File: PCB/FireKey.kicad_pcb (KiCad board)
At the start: 2 copper layers, 3.6 x 3.2 mm, 76 parts, among them SW1 SW_MEC_5E, U1 Arduino_Pro_Micro_USB-C

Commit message: worked on pcb design
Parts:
- moved H7 208.2 mm to (66.0, 58.4)
- moved KEY3 176.0 mm to (196.0, -91.6)
- moved C10 172.5 mm to (233.9, -92.0)
- moved KEY13 155.8 mm to (155.6, -71.4)
- moved KEY9 149.7 mm to (117.2, -51.2)
- moved C4 126.9 mm to (173.1, -29.4)
- moved C1 123.2 mm to (152.2, -11.2)
- moved C15 123.2 mm to (179.6, -35.5)
- moved C3 123.2 mm to (213.9, -71.8)
- moved C7 123.2 mm to (233.9, -89.5)
- moved C8 123.2 mm to (152.2, -8.69)
- moved C9 123.2 mm to (157.9, -14.5)
- moved D10 123.2 mm to (206.5, -62.0)
- moved D2 123.2 mm to (168.0, -29.0)
- moved D5 123.2 mm to (192.2, -54.5)
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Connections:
- KEY1 pad 1: Net-(D1-Pad2) -> Net-(D3-Pad2)
- KEY1 pad 2: Net-(D1-Pad2) -> Net-(D3-Pad2)
- KEY13 pad 1: Net-(D13-Pad2) -> Net-(D15-Pad2)
- KEY13 pad 2: Net-(D13-Pad2) -> Net-(D15-Pad2)
- KEY15 pad 1: Net-(D15-Pad2) -> Net-(D13-Pad2)
- KEY15 pad 2: Net-(D15-Pad2) -> Net-(D13-Pad2)
- KEY3 pad 1: Net-(D3-Pad2) -> Net-(D1-Pad2)
- KEY3 pad 2: Net-(D3-Pad2) -> Net-(D1-Pad2)
- KEY7 pad 1: Net-(D7-Pad2) -> Net-(D9-Pad2)
- KEY7 pad 2: Net-(D7-Pad2) -> Net-(D9-Pad2)
- KEY9 pad 1: Net-(D9-Pad2) -> Net-(D7-Pad2)
- KEY9 pad 2: Net-(D9-Pad2) -> Net-(D7-Pad2)
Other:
- board size 3.6 x 3.2 mm -> 100 x 96.5 mm

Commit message: worked on pcb design
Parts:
- moved H8 228.8 mm to (119.4, 143.5)
- moved H6 198.3 mm to (57.1, 99.1)
- moved H11 179.3 mm to (149.5, 143.5)
- moved H9 175.1 mm to (57.1, 143.5)
- moved H12 109.2 mm to (119.4, 54.6)
- moved H5 73.0 mm to (196.8, 22.9)
- moved H10 66.5 mm to (149.5, 54.6)
- moved H7 9.67 mm to (57.1, 54.6)
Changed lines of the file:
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@@
   )
   (footprint "MountingHole:MountingHole_3.2mm_M3" (layer "F.Cu")
-    (at 185.305 -52.225)
+    (at 57.15 99.06)
     (descr "Mounting Hole 3.2mm, no annular, M3")
     (tags "mounting hole 3.2mm no annular m3")
@@
     (property "exclude_from_bom" "")
     (attr exclude_from_pos_files exclude_from_bom)
-    (fp_text reference "H6" (at 0 -4.2) (layer "F.SilkS")
+    (fp_text reference "H6" (at 0 -4.2) (layer "F.SilkS") hide
       (effects (font (size 1 1) (thickness 0.15)))
     )
@@
   )
   (footprint "MountingHole:MountingHole_3.2mm_M3" (layer "F.Cu")
-    (at 138.055 -11.825)
+    (at 57.15 143.51)
     (descr "Mounting Hole 3.2mm, no annular, M3")
     (tags "mounting hole 3.2mm no annular m3")
@@
     (property "exclude_from_bom" "")
     (attr exclude_from_pos_files exclude_from_bom)
-    (fp_text reference "H9" (at 0 -4.2) (layer "F.SilkS")
+    (fp_text reference "H9" (at 0 -4.2) (layer "F.SilkS") hide
       (effects (font (size 1 1) (thickness 0.15)))
     )
@@
   )
   (footprint "MountingHole:MountingHole_3.2mm_M3" (layer "F.Cu")
-    (at 66.04 58.42)
+    (at 57.15 54.61)
     (descr "Mounting Hole 3.2mm, no annular, M3")
     (tags "mounting hole 3.2mm no annular m3")
@@
   )
   (footprint "MountingHole:MountingHole_3.2mm_M3" (layer "F.Cu")
-    (at 207.575 -67.625)
+    (at 119.38 143.51)
     (descr "Mounting Hole 3.2mm, no annular, M3")
     (tags "mounting hole 3.2mm no annular m3")
@@
     (property "exclude_from_bom" "")
     (attr exclude_from_pos_files exclude_from_bom)
-    (fp_text reference "H8" (at 0 -4.2) (layer "F.SilkS")
+    (fp_text reference "H8" (at 0 -4.2) (layer "F.SilkS") hide
       (effects (font (size 1 1) (thickness 0.15)))
     )
@@
   )
   (footprint "MountingHole:MountingHole_3.2mm_M3" (layer "F.Cu")
-    (at 177.205 -47.425)
+    (at 196.85 22.86)
     (descr "Mounting Hole 3.2mm, no annular, M3")
     (tags "mounting hole 3.2mm no annular m3")
@@
     (property "exclude_from_bom" "")
     (attr exclude_from_pos_files exclude_from_bom)
-    (fp_text reference "H5" (at 0 -4.2) (layer "F.SilkS")
+    (fp_text reference "H5" (at 0 -4.2) (layer "F.SilkS") hide
       (effects (font (size 1 1) (thickness 0.15)))
     )
@@
   )
   (footprint "MountingHole:MountingHole_3.2mm_M3" (layer "F.Cu")
-    (at 146.005 -11.825)
+    (at 149.51 54.61)
     (descr "Mounting Hole 3.2mm, no annular, M3")
     (tags "mounting hole 3.2mm no annular m3")
@@
     (property "exclude_from_bom" "")
     (attr exclude_from_pos_files exclude_from_bom)
-    (fp_text reference "H10" (at 0 -4.2) (layer "F.SilkS")
+    (fp_text reference "H10" (at 0 -4.2) (layer "F.SilkS") hide
       (effects (font (size 1 1) (thickness 0.15)))
     )
@@
   )
   (footprint "MountingHole:MountingHole_3.2mm_M3" (layer "F.Cu")
-    (at 169.105 -42.625)
+    (at 119.38 54.61)
     (descr "Mounting Hole 3.2mm, no annular, M3")
     (tags "mounting hole 3.2mm no annular m3")
@@
     (property "exclude_from_bom" "")
     (attr exclude_from_pos_files exclude_from_bom)
-    (fp_text reference "H12" (at 0 -4.2) (layer "F.SilkS")
+    (fp_text reference "H12" (at 0 -4.2) (layer "F.SilkS") hide
       (effects (font (size 1 1) (thickness 0.15)))
     )
@@
   )
   (footprint "MountingHole:MountingHole_3.2mm_M3" (layer "F.Cu")
-    (at 169.105 -34.675)
+    (at 149.51 143.51)
     (descr "Mounting Hole 3.2mm, no annular, M3")
     (tags "mounting hole 3.2mm no annular m3")
@@
     (property "exclude_from_bom" "")
     (attr exclude_from_pos_files exclude_from_bom)
-    (fp_text reference "H11" (at 0 -4.2) (layer "F.SilkS")
+    (fp_text reference "H11" (at 0 -4.2) (layer "F.SilkS") hide
       (effects (font (size 1 1) (thickness 0.15)))
     )
@@
     )
   )
-  (gr_arc locked (start 55.88 147.32) (mid 53.75868 146.44132) (end 52.88 144.32) (layer "Edge.Cuts") (width 0.2))
-  (gr_line locked (start 55.88 50.8) (end 149.86 50.8) (layer "Edge.Cuts") (width 0.2))
-  (gr_line locked (start 152.86 144.32) (end 152.86 53.8) (layer "Edge.Cuts") (width 0.2))
-  (gr_arc locked (start 149.86 50.8) (mid 151.98132 51.67868) (end 152.86 53.8) (layer "Edge.Cuts") (width 0.2))
-  (gr_arc locked (start 152.86 144.32) (mid 151.98132 146.44132) (end 149.86 147.32) (layer "Edge.Cuts") (width 0.2))
-  (gr_line locked (start 149.86 147.32) (end 55.88 147.32) (layer "Edge.Cuts") (width 0.2))
-  (gr_arc locked (start 52.88 53.8) (mid 53.75868 51.67868) (end 55.88 50.8) (layer "Edge.Cuts") (width 0.2))
-  (gr_line locked (start 52.88 53.8) (end 52.88 144.32) (layer "Edge.Cuts") (width 0.2))
+  (gr_arc locked (start 56.34 147.32) (mid 54.21868 146.44132) (end 53.34 144.32) (layer "Edge.Cuts") (width 0.2))
+  (gr_line locked (start 56.34 50.8) (end 150.32 50.8) (layer "Edge.Cuts") (width 0.2))
+  (gr_line locked (start 153.32 144.32) (end 153.32 53.8) (layer "Edge.Cuts") (width 0.2))
+  (gr_arc locked (start 150.32 50.8) (mid 152.44132 51.67868) (end 153.32 53.8) (layer "Edge.Cuts") (width 0.2))
+  (gr_arc locked (start 153.32 144.32) (mid 152.44132 146.44132) (end 150.32 147.32) (layer "Edge.Cuts") (width 0.2))
+  (gr_line locked (start 150.32 147.32) (end 56.34 147.32) (layer "Edge.Cuts") (width 0.2))
+  (gr_arc locked (start 53.34 53.8) (mid 54.21868 51.67868) (end 56.34 50.8) (layer "Edge.Cuts") (width 0.2))
+  (gr_line locked (start 53.34 53.8) (end 53.34 144.32) (layer "Edge.Cuts") (width 0.2))
 )

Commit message: moved main components on pcb
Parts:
- H10, H11, H12, H5, H6, H7, H8, H9: value M3_MountingHole -> M3_Hole
- moved KEY14 229.4 mm to (90.2, 132.1)
- moved KEY4 220.9 mm to (71.1, 74.9)
- moved KEY12 215.2 mm to (109.2, 113.0)
- moved KEY10 212.1 mm to (71.1, 113.0)
- moved KEY11 209.6 mm to (90.2, 113.0)
- moved KEY13 208.7 mm to (109.2, 132.1)
- moved OLED1 203.0 mm to (134.6, 121.9)
- moved KEY8 196.8 mm to (90.2, 94.0)
- moved KEY3 193.3 mm to (71.1, 55.9)
- moved KEY15 169.4 mm to (71.1, 132.1)
- moved KEY9 152.3 mm to (71.1, 94.0)
- moved KEY6 148.6 mm to (109.2, 74.9)
- moved KEY5 134.7 mm to (90.2, 74.9)
- moved KEY7 128.1 mm to (109.2, 94.0)
- moved KEY2 126.5 mm to (90.2, 55.9)
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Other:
- board text added: "JLCJLCJLCJLC"

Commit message: worked on placing parts on pcb
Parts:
- C1, C10, C11, C12, C13, C14, C15, C2, C3, C4, C5, C6, C7, C8, C9, D1, D10, D11, D12, D13, D14, D15, D2, D3, D4, D5, D6, D7, D8, D9, LED1, LED10, LED11, LED12, LED13, LED14, LED15, LED2, LED3, LED4, LED5, LED6, LED7, LED8, LED9, R1: moved to B.Cu
- moved C10 268.2 mm to (75.8, 124.6)
- moved LED10 242.0 mm to (68.6, 123.8)
- moved C7 235.6 mm to (99.4, 104.0), turned to 180 degrees
- moved C11 235.5 mm to (94.9, 124.6)
- moved LED15 224.9 mm to (68.6, 142.9), turned to 180 degrees
- moved C15 213.7 mm to (62.1, 143.0), turned to -90 degrees
- moved C5 213.1 mm to (94.9, 86.5)
- moved C2 209.0 mm to (80.4, 65.9), turned to 180 degrees
- moved D13 206.6 mm to (186.7, 106.0), turned to 180 degrees
- moved C3 205.5 mm to (61.3, 65.9), turned to 180 degrees
- moved LED13 202.0 mm to (106.7, 142.9), turned to 180 degrees
- moved D8 196.0 mm to (192.4, 106.0), turned to 180 degrees
- moved C13 190.8 mm to (99.4, 142.1), turned to 180 degrees
- moved C14 189.3 mm to (80.4, 142.1), turned to 180 degrees
- moved LED12 188.5 mm to (106.7, 123.8)
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
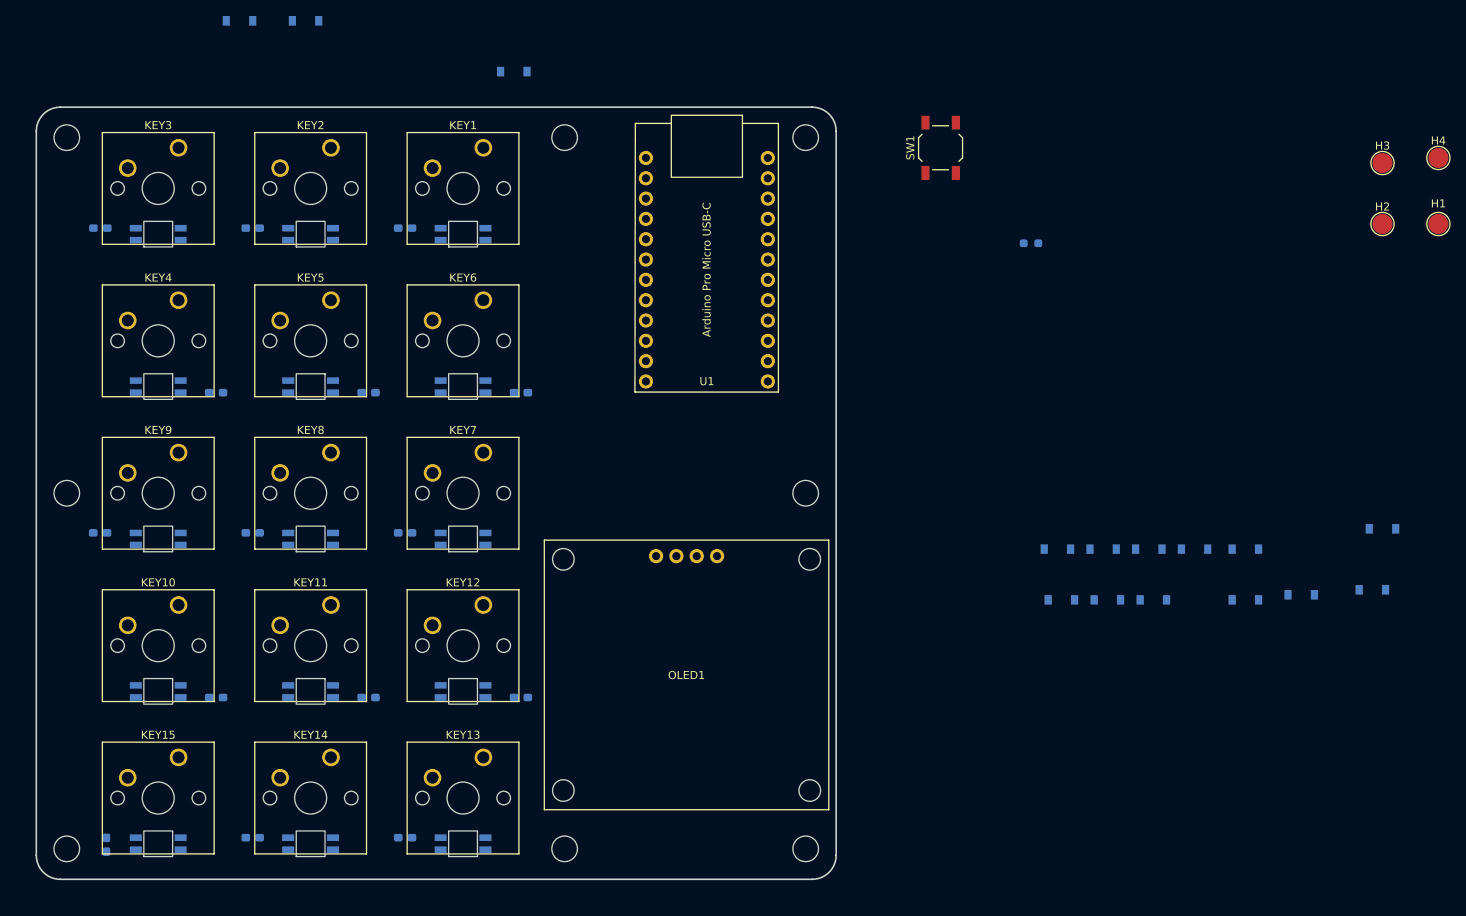
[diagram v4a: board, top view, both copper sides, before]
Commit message: placed all parts on pcb
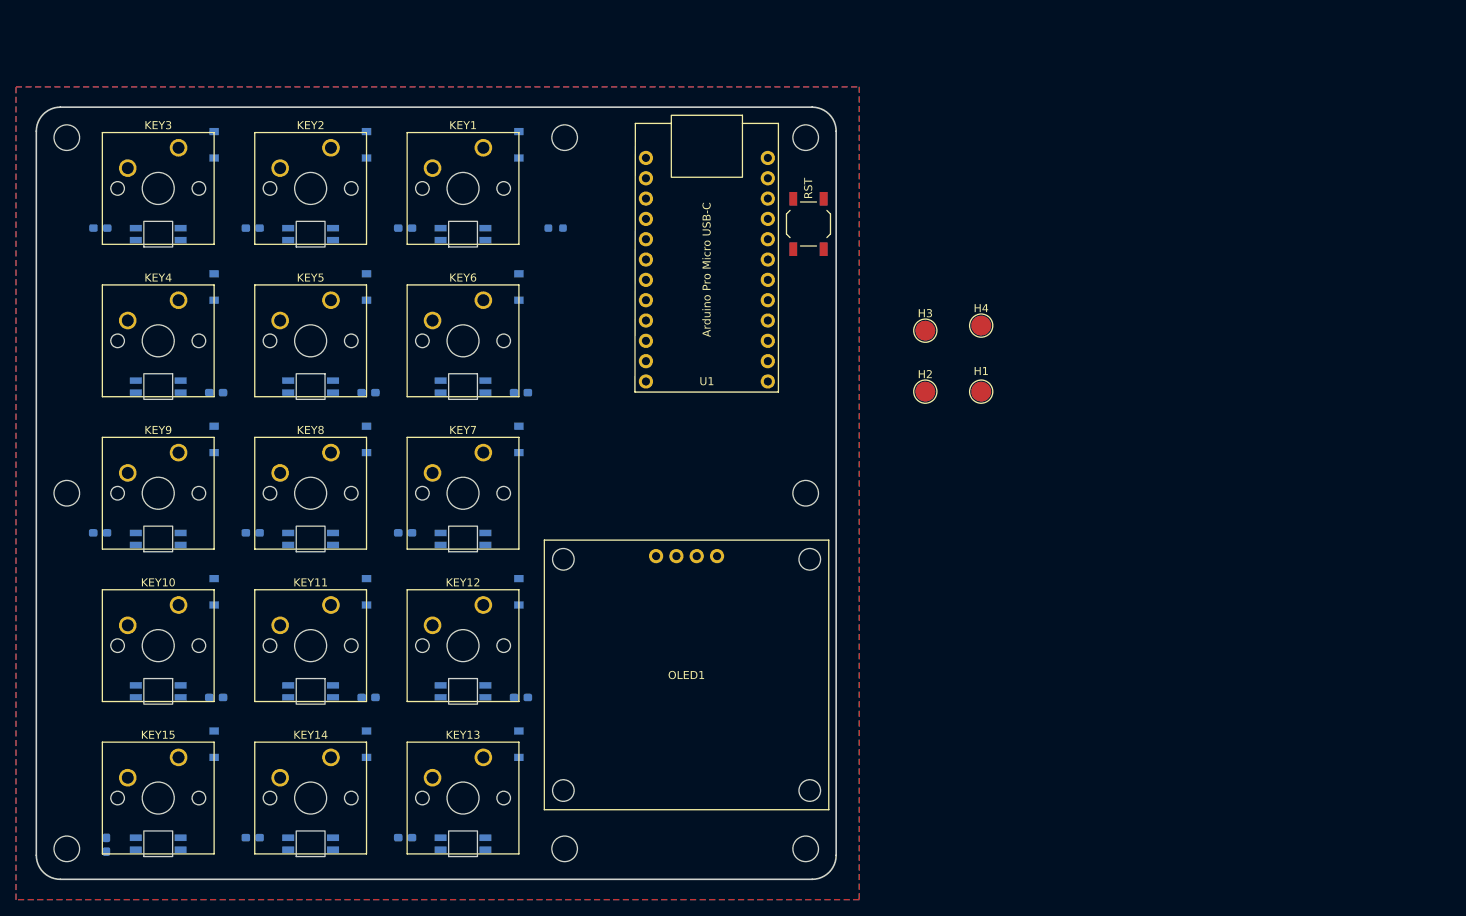
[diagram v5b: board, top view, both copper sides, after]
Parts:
- moved D4 149.6 mm to (75.6, 73.3), turned to -90 degrees
- moved D5 123.0 mm to (94.6, 73.3), turned to -90 degrees
- moved D15 113.8 mm to (75.6, 130.4), turned to -90 degrees
- moved D9 113.4 mm to (75.6, 92.3), turned to -90 degrees
- moved D14 111.3 mm to (94.6, 130.4), turned to -90 degrees
- moved D13 111.3 mm to (113.7, 130.4), turned to -90 degrees
- moved D11 110.0 mm to (94.6, 111.4), turned to -90 degrees
- moved D10 105.5 mm to (75.6, 111.4), turned to -90 degrees
- moved D8 98.7 mm to (94.6, 92.3), turned to -90 degrees
- moved D6 90.6 mm to (113.7, 73.3), turned to -90 degrees
- moved D7 81.8 mm to (113.7, 92.3), turned to -90 degrees
- moved D12 67.8 mm to (113.7, 111.4), turned to -90 degrees
- moved H1 60.9 mm to (171.4, 86.4)
- moved H2 60.9 mm to (164.5, 86.4)
- moved H3 60.9 mm to (164.5, 78.7)
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- renumbered D3 to D1, D15 to D13, D13 to D15, D1 to D3, D9 to D7, D7 to D9
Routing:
- added copper zone on B.Cu, net GND
- added copper zone on F.Cu, net GND
